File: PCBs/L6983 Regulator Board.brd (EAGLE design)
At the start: 54 x 56 mm, 23 parts

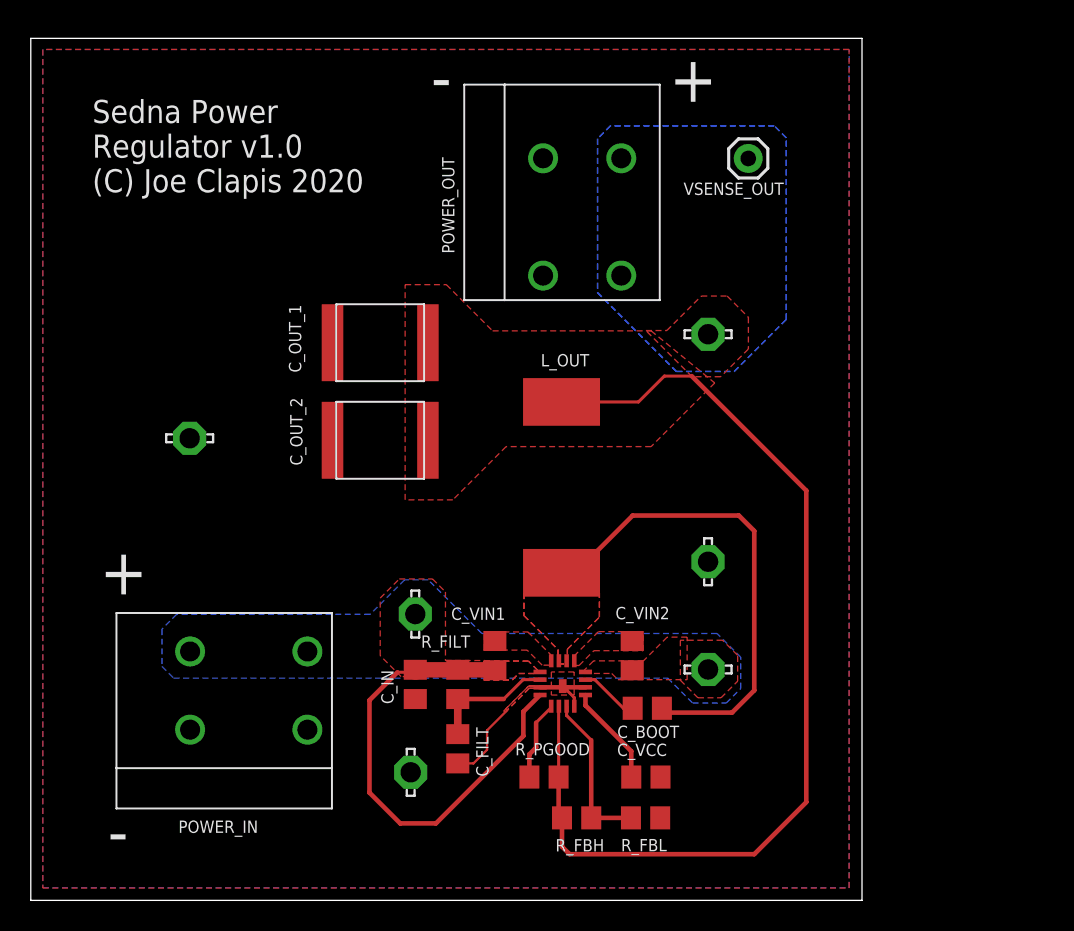
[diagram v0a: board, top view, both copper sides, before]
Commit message: Now that the laser engraver is done, I can start fabricating some boards. Updated the power board to v1.1, put together a BOM to make 3 of them at 12v, 7.2v, and 5v.
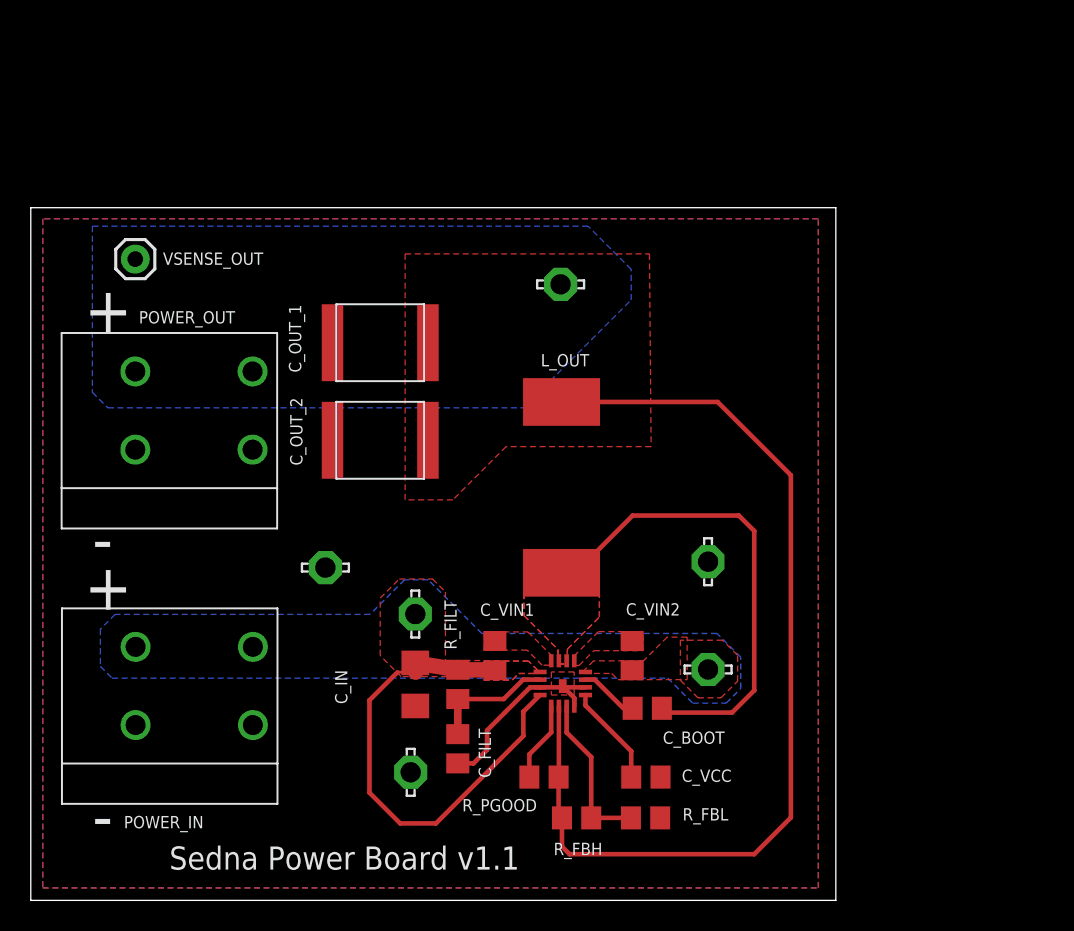
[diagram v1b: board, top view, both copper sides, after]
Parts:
- C_IN: device rcl:C0805 -> rcl:C1206
- moved VSENSE_OUT 40.4 mm to (6.79, 41.7)
- moved POWER_OUT 28.2 mm to (10.6, 31.8), turned to 270 degrees
- moved GND_VIA1 12.2 mm to (19.1, 21.6)
- moved VOUT_VIA 10.1 mm to (34.4, 40.0)
- moved POWER_IN 3.55 mm to (10.6, 13.9)
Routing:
- net GND: track 9.85 -> 12.8 mm
- net V_OUT: track 66.6 -> 64.4 mm
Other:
- board size 54 x 56 mm -> 52.3 x 45 mm
- board text added: "Sedna Power Board v1.1"
- board text removed: "Sedna Power Regulator v1.0 (C) Joe Clapis 2020"

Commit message: Redid the power board layout, trying a thinner but longer variant which should help cable management.
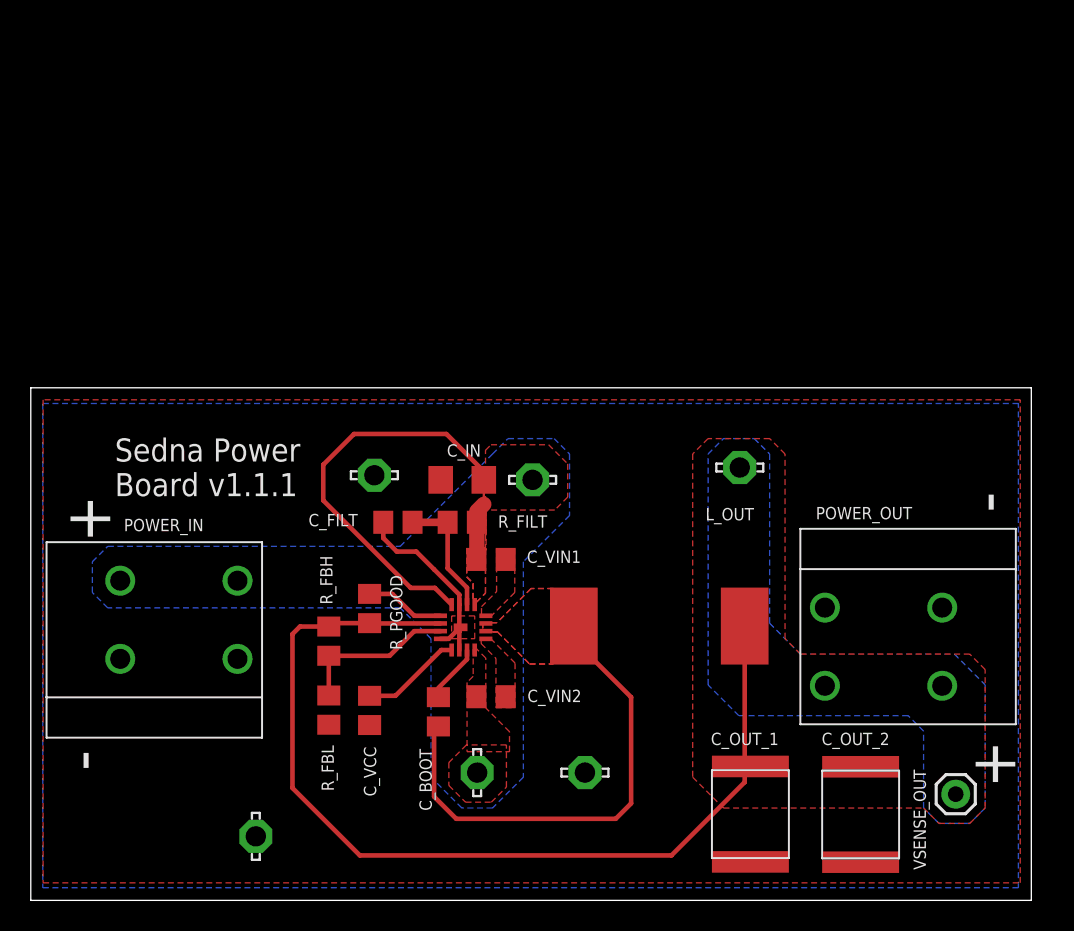
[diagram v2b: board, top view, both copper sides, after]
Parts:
- moved VSENSE_OUT 63.6 mm to (60.1, 6.90), turned to 180 degrees
- moved POWER_OUT 47.4 mm to (55.4, 16.5), turned to 90 degrees
- moved C_OUT_2 39.6 mm to (53.9, 5.58), turned to 270 degrees
- moved C_OUT_1 38.9 mm to (46.8, 5.60), turned to 270 degrees
- moved R_FBL 21.7 mm to (19.4, 12.4), turned to 270 degrees
- moved R_FBH 19.8 mm to (19.4, 16.8), turned to 270 degrees
- moved GND_VIA2 19.4 mm to (22.3, 27.6), turned to 0 degrees
- moved C_VCC 18.5 mm to (22.0, 12.3), turned to 270 degrees
- moved GND_VIA1 18.0 mm to (14.6, 4.16), turned to 270 degrees
- moved VOUT_VIA 16.6 mm to (46.1, 28.1)
- moved VIN_VIA2 16.4 mm to (29.0, 8.30), turned to 270 degrees
- moved GND_VIA3 15.9 mm to (36.0, 8.30), turned to 0 degrees
- moved R_PGOOD 15.8 mm to (22.0, 19.0), turned to 270 degrees
- moved C_FILT 15.2 mm to (23.9, 24.6), turned to 180 degrees
- moved C_IN 13.6 mm to (28.0, 27.3), turned to 180 degrees
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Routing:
- net V_OUT: track 64.4 -> 63.2 mm
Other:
- board size 52.3 x 45 mm -> 65 x 33.3 mm
- board text added: "Sedna Power Board v1.1.1"
- board text removed: "Sedna Power Board v1.1"
